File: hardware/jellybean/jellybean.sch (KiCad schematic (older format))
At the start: 38 parts

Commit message: added cpld
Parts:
- added U?: GSG-XC2C64A-7VQG100C, symbol GSG-XC2C64A-7VQG100C
- P?: value JTAG -> LPC_JTAG
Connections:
- net SGPIO10: now also U?.71 (BANK2F3M11)
- net SGPIO11: now also U?.70 (BANK2F3M12)
- net SGPIO12: now also U?.69 (GND)
- net SGPIO14: now also U?.76 (BANK2F3M8)
- net SGPIO15: now also U?.74 (BANK2F3M9)
- net SGPIO4: now also U?.67 (BANK2F3M14)
- net SGPIO5: now also U?.64 (BANK2F3M15)
- net SGPIO6: now also U?.61 (BANK2F3M16)
- net SGPIO7: now also U?.72 (BANK2F3M10)
- net SGPIO8: now also U?.68 (BANK2F3M13)
- new net DA0: U?.43 (BANK1F4M8)
- new net DA1: U?.42 (BANK1F4M7)
- new net DA2: U?.41 (BANK1F4M6)
- new net DA3: U?.40 (BANK1F4M5)
- new net DA4: U?.39 (BANK1F4M4)
- new net DA5: U?.37 (BANK1F4M3)
- new net DA6: U?.36 (BANK1F4M2)
- new net DA7: U?.35 (BANK1F4M1)
- new net DD0: U?.34 (BANK1F2M16)
- new net DD1: U?.33 (BANK1F2M15)
- new net DD2: U?.32 (BANK1F2M14)
- new net DD3: U?.31 (GND)
- new net DD4: U?.30 (BANK1F2M13)
- new net DD5: U?.29 (BANK1F2M12)
- new net DD6: U?.28 (BANK1F2M11)
- new net DD7: U?.24 (BANK1F2M9)
- new net DD8: U?.19 (BANK1F2M6)
- new net DD9: U?.18 (BANK1F2M5)
- new net GCK0: U?.22 (BANK1F2M7)
- new net GCK1: U?.23 (BANK1F2M8)
- new net GCK2: U?.27 (BANK1F2M10)
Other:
- moved on the sheet: C?, FB?, J?, P?, R?, U?

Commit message: ADC/DAC connector, CPLD power
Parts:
- added C? (x7): 100nF, symbol C
- added K?: CONN_3, symbol CONN_3
- added P?: ADC/DAC, symbol CONN_20X2
- added R? (x10): 100, symbol R
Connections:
- net DA0: now also P?.4 (P4)
- net DA1: now also P?.6 (P6)
- net DA2: now also P?.8 (P8)
- net DA3: now also P?.10 (P10)
- net DA4: now also P?.12 (P12)
- net DA5: now also P?.14 (P14)
- net DA6: now also P?.16 (P16)
- net DA7: now also P?.18 (P18)
- net DD0: now also R?.1
- net DD1: now also R?.1
- net DD2: now also R?.1
- net DD3: now also R?.1
- net DD4: now also R?.1
- net DD5: now also R?.1
- net DD6: now also R?.1
- net DD7: now also R?.1
- net DD8: now also R?.1
- net DD9: now also R?.1
- net GCK0: now also P?.40 (P40)
- net GND: now also C?.2, C?.2, C?.2, C?.2, C?.2, C?.2, C?.2, P?.1 (P1), P?.11 (P11), P?.13 (P13), P?.15 (P15), P?.17 (P17), P?.19 (P19), P?.2 (P2), P?.21 (P21), P?.23 (P23), P?.25, P?.27 (P27), P?.29 (P29), P?.3 (P3), P?.31 (P31), P?.33 (P33), P?.35 (P35), P?.37 (P37), P?.39 (P39), P?.5 (P5), P?.7 (P7), P?.9 (P9)
- net VCC: now also U?.38 (VCCIO1), U?.4 (BANK2F1M9), U?.51 (VCCIO1), C?.1, C?.1, C?.1, K?.1 (P1)
- net +1.8V: now reaches U?.26 (VCC)
- net +1.8V: now also U?.57 (VCC), C?.1, C?.1, K?.3 (P3)
- net VCCIO2: now reaches U?.88 (VCCIO2)
- net VCCIO2: now also U?.98 (VCCIO2), C?.1, C?.1, K?.2 (PM)
- new net: P?.20 (P20), R?.2
- new net: P?.22 (P22), R?.2
- new net: P?.24 (P24), R?.2
- new net: P?.26 (P26), R?.2
- new net: P?.28 (P28), R?.2
- new net: P?.30 (P30), R?.2
- new net: P?.32 (P32), R?.2
- new net: P?.34 (P34), R?.2
- new net: P?.36 (P36), R?.2
- new net: P?.38 (P38), R?.2

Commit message: VAUX fix
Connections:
- net VCC: now also U?.5 (VAUX); no longer U?.4 (BANK2F1M9)

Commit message: voltage regulator
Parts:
- added C? (x5): 10uF, symbol C
- added C?: 22pF, symbol C
- added L? (x2): 4u7, symbol INDUCTOR
- added R?: 634k, symbol R
- added R?: 360k, symbol R
- added R? (x2): 180k, symbol R
- added R? (x2): DNP, symbol R
- added R? (x3): 10k, symbol R
- added U?: TPS62410, symbol TPS62410
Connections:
- net +1.8V: now also C?.1, C?.1, C?.1, L?.2, R?.1
- net GND: now also C?.1, C?.1, C?.2, C?.2, C?.2, R?.1, R?.1, R?.1, R?.2, U?.0 (PP), U?.8 (GND)
- net VBUS: now also C?.1, R?.1, U?.3 (VIN)
- net VCC: now also C?.2, C?.2, L?.1, R?.1, R?.1, U?.4 (FB1)
- net EN1V8: now reaches U?.105 (P2_11)
- net EN1V8: now also R?.2, U?.9 (EN2)
- net VREGMODE: now reaches U?.106 (P2_12)
- net VREGMODE: now also R?.1
- new net: C?.2, R?.2, R?.2, U?.1 (ADJ2)
- new net: L?.1, U?.10 (SW2)
- new net: R?.1, R?.2, R?.2, U?.2 (MODE/DATA)
- new net: R?.2, R?.2, U?.5 (DEF1)
- new net: L?.2, U?.6 (SW1)
- new net: R?.2, U?.7 (EN1)

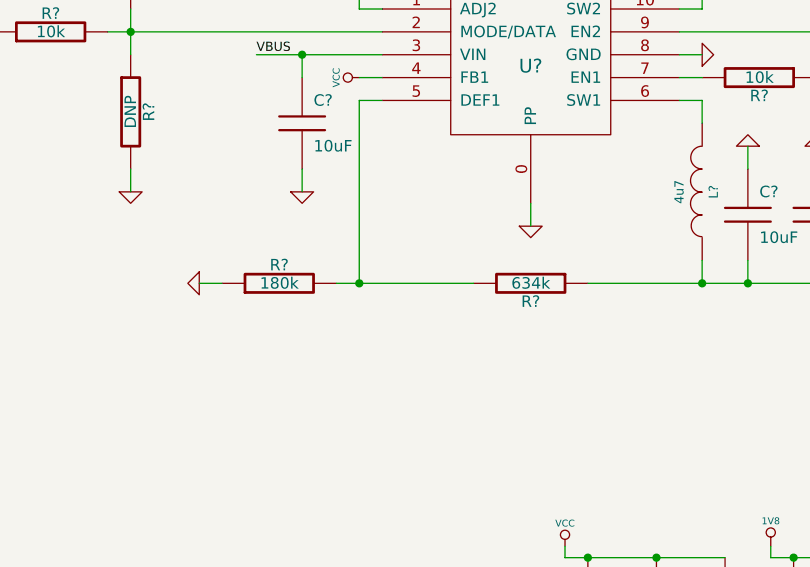
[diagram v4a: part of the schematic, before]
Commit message: better resistor selection for 2.7 V
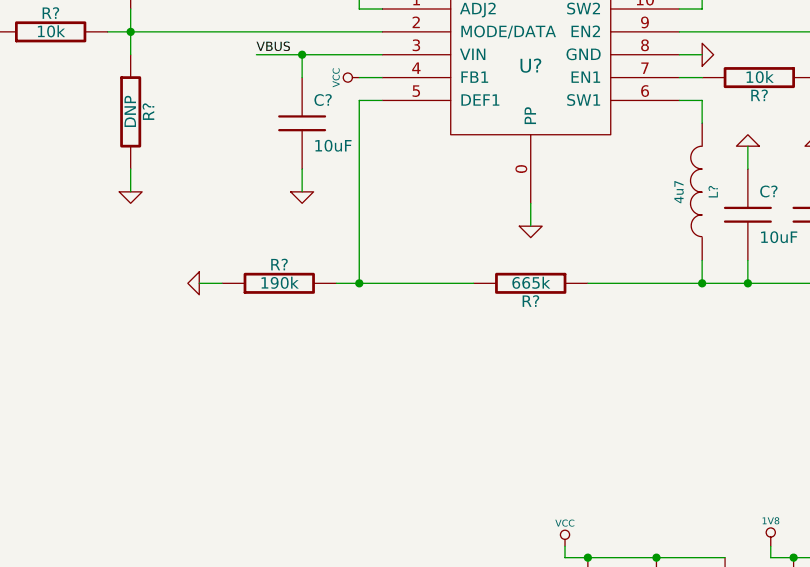
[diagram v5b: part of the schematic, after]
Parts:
- R?: value 634k -> 665k
- R?: value 180k -> 190k
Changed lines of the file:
@@
-EESchema Schematic File Version 2  date Sun Apr  8 21:11:37 2012
+EESchema Schematic File Version 2  date Sun Apr  8 21:29:58 2012
 LIBS:power
 LIBS:device
@@
 P 13150 2650
 F 0 "R?" V 13230 2650 50  0000 C CNN
-F 1 "180k" V 13150 2650 50  0000 C CNN
+F 1 "190k" V 13150 2650 50  0000 C CNN
 	1    13150 2650
 	0    -1   -1   0
@@
 P 14250 2650
 F 0 "R?" V 14330 2650 50  0000 C CNN
-F 1 "634k" V 14250 2650 50  0000 C CNN
+F 1 "665k" V 14250 2650 50  0000 C CNN
 	1    14250 2650
 	0    1    1    0

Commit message: SPI flash
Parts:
- added C?: 100nF, symbol C
- added P?: CONN_6X2, symbol CONN_6X2
- added U?: W25Q80BV, symbol W25Q80BV
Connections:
- net GND: now also C?.2, U?.4 (GND)
- net SPIFI_SIO2: now also P?.12
- net SPIFI_SIO3: now also P?.10
- net SSP0_MISO: now also P?.2 (P2)
- net SSP0_MOSI: now also P?.4 (P4)
- net SSP0_SCK: now also P?.6 (P6)
- net SSP0_SSEL: now also P?.8 (P8)
- net VCC: now also C?.1, U?.8 (VCC)
- new net: P?.7 (P7), U?.1 (CS)
- new net: P?.1 (P1), U?.2 (DO)
- new net: P?.11, U?.3 (WP)
- new net: P?.3 (P3), U?.5 (DI)
- new net: P?.5 (P5), U?.6 (CLK)
- new net: P?.9, U?.7 (HOLD)
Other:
- moved on the sheet: C?, L?, R?, U?

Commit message: rearranged some pins
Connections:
- net DD3: now also U?.30 (BANK1F2M13); no longer U?.31 (GND)
- net DD4: now also U?.29 (BANK1F2M12); no longer U?.30 (BANK1F2M13)
- net DD5: now also U?.28 (BANK1F2M11); no longer U?.29 (BANK1F2M12)
- net DD6: now also U?.24 (BANK1F2M9); no longer U?.28 (BANK1F2M11)
- net DD7: now also U?.19 (BANK1F2M6); no longer U?.24 (BANK1F2M9)
- net DD8: now also U?.18 (BANK1F2M5); no longer U?.19 (BANK1F2M6)
- net DD9: now also U?.17 (BANK1F2M4); no longer U?.18 (BANK1F2M5)
- net GND: now also U?.100 (GND), U?.21 (GND), U?.31 (GND), U?.62 (GND), U?.69 (GND), U?.84 (GND)
- net SGPIO0: now also U?.89 (BANK2F3M3)
- net SGPIO1: now also U?.79 (BANK2F3M5)
- net SGPIO10: now also U?.76 (BANK2F3M8); no longer U?.71 (BANK2F3M11)
- net SGPIO11: now also U?.71 (BANK2F3M11); no longer U?.70 (BANK2F3M12)
- net SGPIO12: now also U?.70 (BANK2F3M12); no longer U?.69 (GND)
- net SGPIO13: now also U?.15 (P4_8), U?.90 (BANK2F3M2); no longer U?.70 (P1_20)
- net SGPIO14: now also U?.81 (BANK2F3M4); no longer U?.76 (BANK2F3M8)
- net SGPIO15: now also U?.78 (BANK2F3M6); no longer U?.74 (BANK2F3M9)
- net SGPIO2: now also U?.74 (BANK2F3M9)
- net SGPIO3: now also U?.72 (BANK2F3M10)
- net SGPIO7: now also U?.77 (BANK2F3M7); no longer U?.72 (BANK2F3M10)
- net SGPIO9: now also U?.91 (BANK2F3M1)
- net SSP1_SCK: now reaches U?.68 (P1_19)
- net SD_RST renamed SSP1_MISO
- net SD_VOLT1 renamed SSP1_MOSI
- new net SSP1_SSEL: U?.70 (P1_20)
- no-connect marks 30 -> 28

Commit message: labeled SCT pins for expansion
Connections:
- net EN1V8: now also U?.100 (P6_10); no longer U?.105 (P2_11)
- net VREGMODE: now also U?.101 (P6_11); no longer U?.106 (P2_12)
- net CTOUT_7: now reaches U?.103 (P6_12)
- net CTOUT_2: now reaches U?.104 (P2_10)
- net CTIN_4: now reaches U?.108 (P2_13)
- net CTOUT_14: now reaches U?.110 (P7_0)
- net CTOUT_15: now reaches U?.112 (P3_0)
- net CTIN_3: now reaches U?.117 (P7_3)
- net CTOUT_1: now reaches U?.3 (P4_1)
- net CTOUT_0: now reaches U?.8 (P4_2)
- net CTIN_6: now reaches U?.80 (P6_4)
- net CTOUT_6: now reaches U?.82 (P6_5)
- net CTIN_2: now reaches U?.91 (P2_5)
- net CTIN_7: now reaches U?.97 (P6_9)
- new net CTOUT_4: U?.106 (P2_12)
- new net CTOUT_5: U?.105 (P2_11)
